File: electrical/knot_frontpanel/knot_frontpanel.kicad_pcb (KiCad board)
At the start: 2 copper layers, 61 x 13 mm, 0 parts

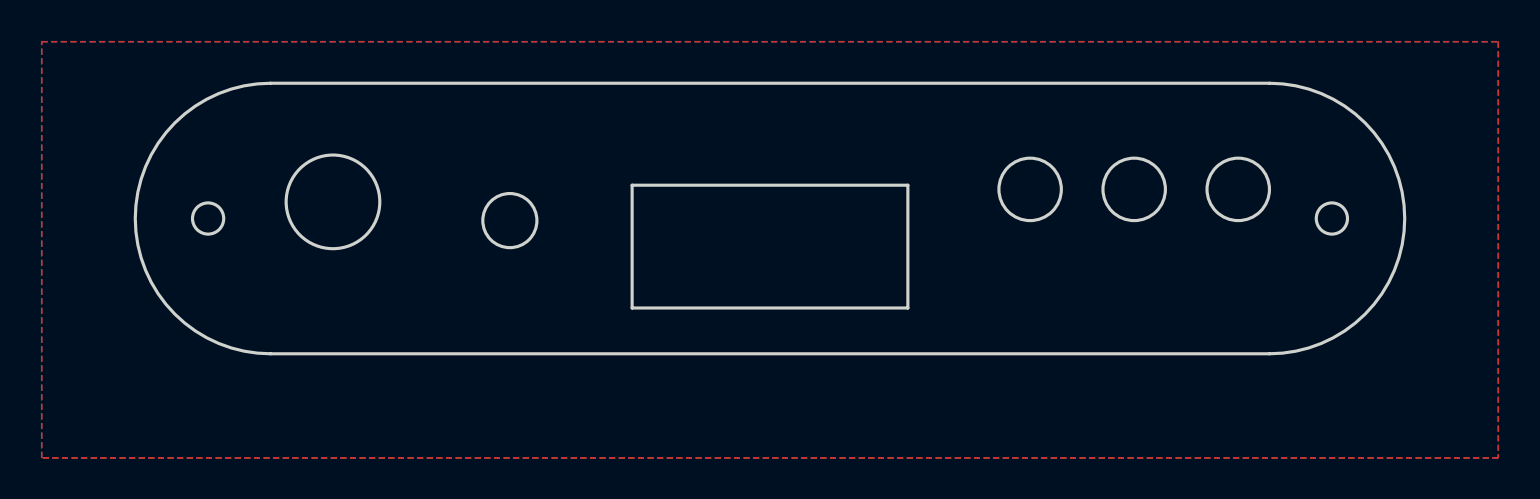
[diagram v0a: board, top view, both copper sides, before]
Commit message: SUKU sync + fw connect status led function added
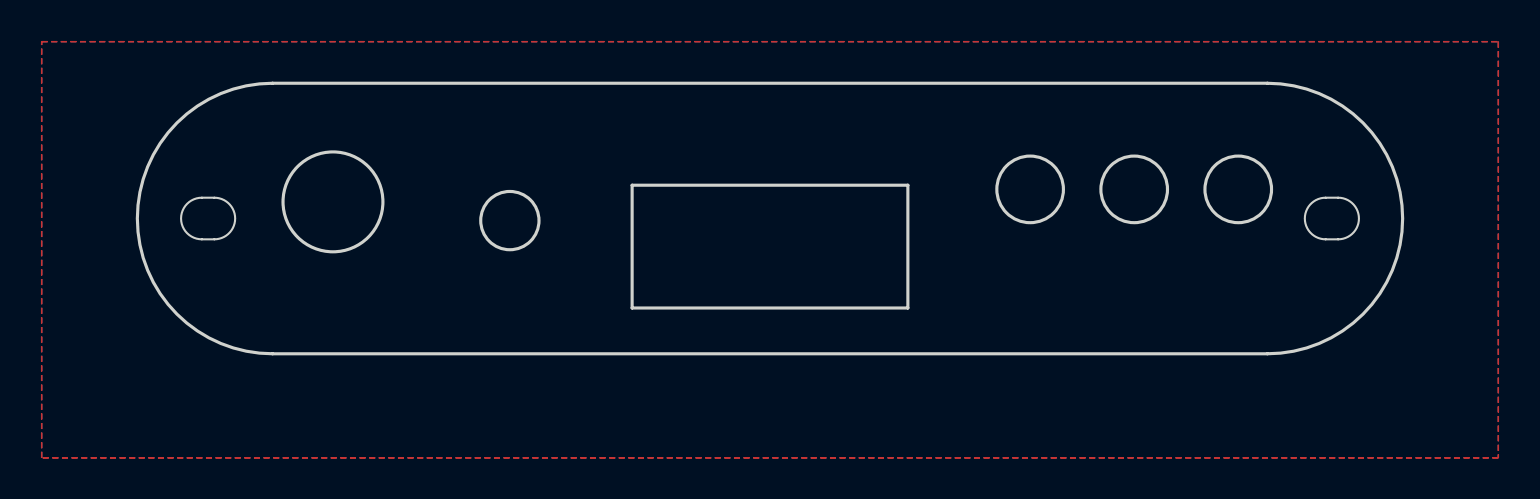
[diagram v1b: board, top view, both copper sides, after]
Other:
- board size 61 x 13 mm -> 60.8 x 13 mm
- board text added: "Frontpanel Inside 2022/10"
- board text removed: "Frontpanel Inside 2022/9"
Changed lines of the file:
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@@
   )
   (net 0 "")
-  (gr_circle (center 79 92.7) (end 81.25 92.7) (layer "Edge.Cuts") (width 0.15) (fill none))
-  (gr_line (start 76 100) (end 124 100) (layer "Edge.Cuts") (width 0.15))
+  (gr_circle (center 79 92.7) (end 81.4 92.7) (layer "Edge.Cuts") (width 0.15) (fill none))
+  (gr_line (start 76.1 100) (end 123.9 100) (layer "Edge.Cuts") (width 0.15))
+  (gr_arc (start 72.7 94.5) (mid 71.7 93.5) (end 72.7 92.5) (layer "Edge.Cuts") (width 0.1))
   (gr_rect (start 93.375 91.9) (end 106.625 97.8) (layer "Edge.Cuts") (width 0.15) (fill none))
-  (gr_arc (start 124 87) (mid 130.5 93.5) (end 124 100) (layer "Edge.Cuts") (width 0.15))
-  (gr_arc (start 76 100) (mid 69.5 93.5) (end 76 87) (layer "Edge.Cuts") (width 0.15))
-  (gr_circle (center 87.5 93.6) (end 88.8 93.6) (layer "Edge.Cuts") (width 0.15) (fill none))
-  (gr_circle (center 122.5 92.1) (end 124 92.1) (layer "Edge.Cuts") (width 0.15) (fill none))
-  (gr_line (start 76 87) (end 124 87) (layer "Edge.Cuts") (width 0.15))
-  (gr_circle (center 73 93.5) (end 73.75 93.5) (layer "Edge.Cuts") (width 0.15) (fill none))
-  (gr_circle (center 127 93.5) (end 127.75 93.5) (layer "Edge.Cuts") (width 0.15) (fill none))
-  (gr_circle (center 112.5 92.1) (end 114 92.1) (layer "Edge.Cuts") (width 0.15) (fill none))
-  (gr_circle (center 117.5 92.1) (end 119 92.1) (layer "Edge.Cuts") (width 0.15) (fill none))
-  (gr_text "Frontpanel Inside 2022/9" (at 100 89) (layer "B.SilkS")
+  (gr_arc (start 127.3 92.5) (mid 128.3 93.5) (end 127.3 94.5) (layer "Edge.Cuts") (width 0.1))
+  (gr_line (start 72.7 92.5) (end 73.3 92.5) (layer "Edge.Cuts") (width 0.1))
+  (gr_line (start 126.7 92.5) (end 127.3 92.5) (layer "Edge.Cuts") (width 0.1))
+  (gr_arc (start 123.9 87) (mid 130.4 93.5) (end 123.9 100) (layer "Edge.Cuts") (width 0.15))
+  (gr_line (start 72.7 94.5) (end 73.3 94.5) (layer "Edge.Cuts") (width 0.1))
+  (gr_arc (start 76.1 100) (mid 69.6 93.5) (end 76.1 87) (layer "Edge.Cuts") (width 0.15))
+  (gr_arc (start 73.3 92.5) (mid 74.3 93.5) (end 73.3 94.5) (layer "Edge.Cuts") (width 0.1))
+  (gr_circle (center 87.5 93.6) (end 88.9 93.6) (layer "Edge.Cuts") (width 0.15) (fill none))
+  (gr_circle (center 122.5 92.1) (end 124.1 92.1) (layer "Edge.Cuts") (width 0.15) (fill none))
+  (gr_line (start 76.1 87) (end 123.9 87) (layer "Edge.Cuts") (width 0.15))
+  (gr_arc (start 126.7 94.5) (mid 125.7 93.5) (end 126.7 92.5) (layer "Edge.Cuts") (width 0.1))
+  (gr_line (start 126.7 94.5) (end 127.3 94.5) (layer "Edge.Cuts") (width 0.1))
+  (gr_circle (center 112.5 92.1) (end 114.1 92.1) (layer "Edge.Cuts") (width 0.15) (fill none))
+  (gr_circle (center 117.5 92.1) (end 119.1 92.1) (layer "Edge.Cuts") (width 0.15) (fill none))
+  (gr_text "Frontpanel Inside 2022/10" (at 100 89) (layer "B.SilkS")
     (effects (font (size 1.5 1.5) (thickness 0.3)) (justify mirror))
   )
